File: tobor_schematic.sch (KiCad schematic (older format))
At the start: 19 parts

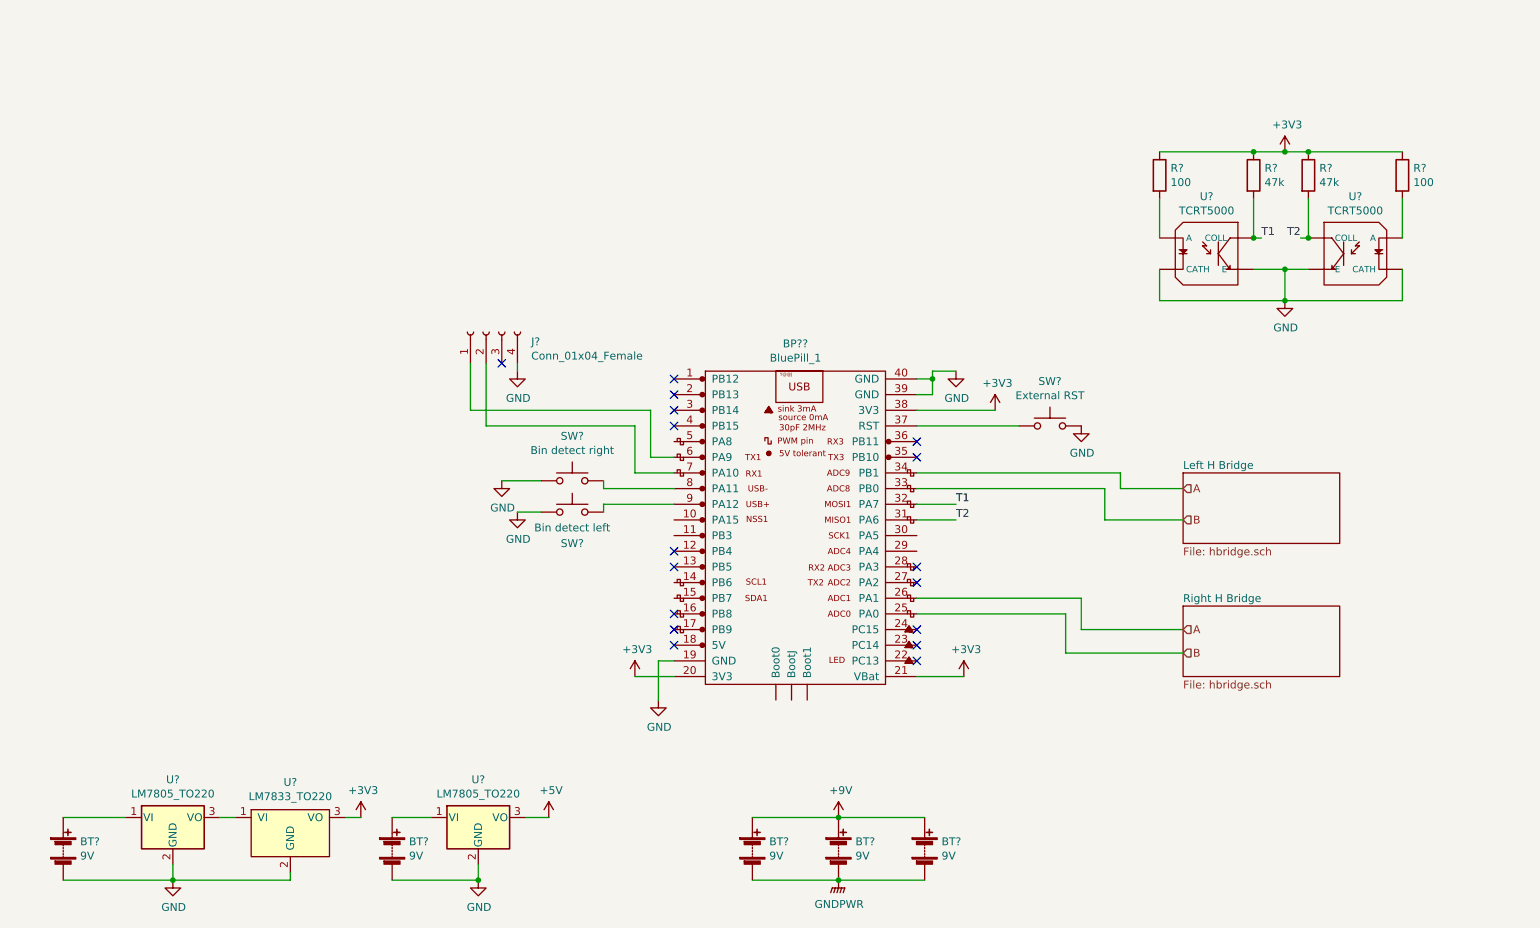
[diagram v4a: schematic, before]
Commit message: Add part numbers
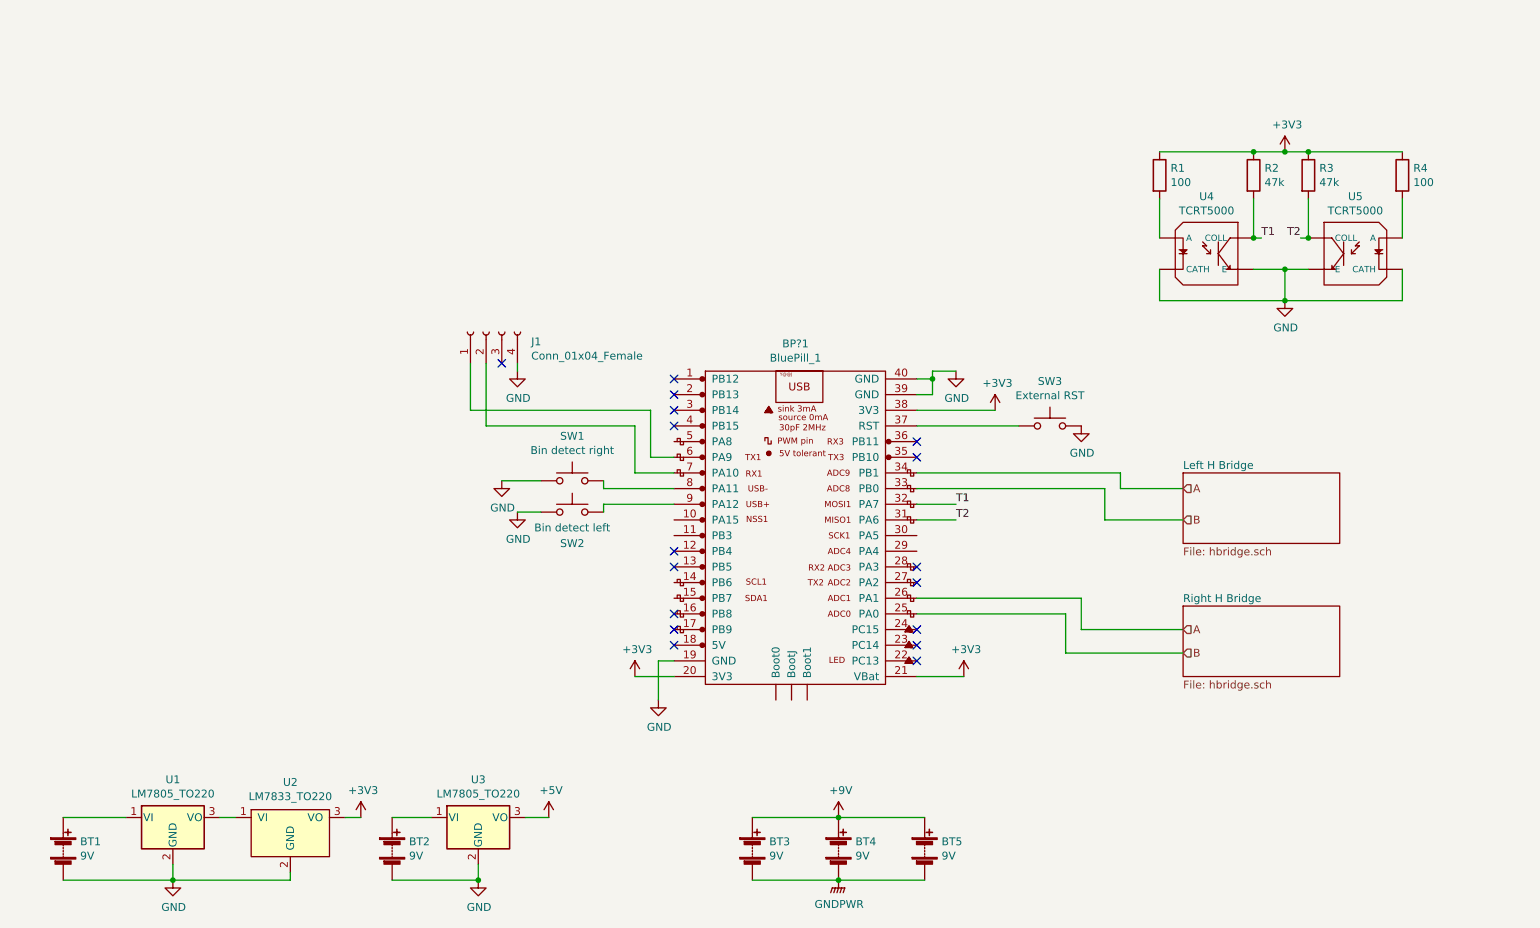
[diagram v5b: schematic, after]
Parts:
- gave numbers to parts that had none: 19
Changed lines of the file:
@@
 $EndDescr
 $Comp
-L Device:Battery BT?
+L Device:Battery BT1
 U 1 1 5EF5BD77
 P 1300 6050
-F 0 "BT?" H 1408 6096 50  0000 L CNN
+F 0 "BT1" H 1408 6096 50  0000 L CNN
 F 1 "9V" H 1408 6005 50  0000 L CNN
 F 2 "" V 1300 6110 50  0001 C CNN
@@
 $EndComp
 $Comp
-L Device:Battery BT?
+L Device:Battery BT3
 U 1 1 5EF5C6C1
 P 5700 6050
-F 0 "BT?" H 5808 6096 50  0000 L CNN
+F 0 "BT3" H 5808 6096 50  0000 L CNN
 F 1 "9V" H 5808 6005 50  0000 L CNN
 F 2 "" V 5700 6110 50  0001 C CNN
@@
 $EndComp
 $Comp
-L Device:Battery BT?
+L Device:Battery BT4
 U 1 1 5EF5C9BC
 P 6250 6050
-F 0 "BT?" H 6358 6096 50  0000 L CNN
+F 0 "BT4" H 6358 6096 50  0000 L CNN
 F 1 "9V" H 6358 6005 50  0000 L CNN
 F 2 "" V 6250 6110 50  0001 C CNN
@@
 $EndComp
 $Comp
-L Device:Battery BT?
+L Device:Battery BT5
 U 1 1 5EF5CE4D
 P 6800 6050
-F 0 "BT?" H 6908 6096 50  0000 L CNN
+F 0 "BT5" H 6908 6096 50  0000 L CNN
 F 1 "9V" H 6908 6005 50  0000 L CNN
 F 2 "" V 6800 6110 50  0001 C CNN
@@
 $EndComp
 $Comp
-L Device:Battery BT?
+L Device:Battery BT2
 U 1 1 5EF5D22E
 P 3400 6050
-F 0 "BT?" H 3508 6096 50  0000 L CNN
+F 0 "BT2" H 3508 6096 50  0000 L CNN
 F 1 "9V" H 3508 6005 50  0000 L CNN
 F 2 "" V 3400 6110 50  0001 C CNN
@@
 Connection ~ 6250 6250
 $Comp
-L Regulator_Linear:LM7805_TO220 U?
+L Regulator_Linear:LM7805_TO220 U1
 U 1 1 5EF5FC3A
 P 2000 5850
-F 0 "U?" H 2000 6092 50  0000 C CNN
+F 0 "U1" H 2000 6092 50  0000 C CNN
 F 1 "LM7805_TO220" H 2000 6001 50  0000 C CNN
 F 2 "Package_TO_SOT_THT:TO-220-3_Vertical" H 2000 6075 50  0001 C CIN
@@
 	2000 6250 2000 6150
 $Comp
-L Regulator_Linear:LM7805_TO220 U?
+L Regulator_Linear:LM7805_TO220 U3
 U 1 1 5EF6637D
 P 3950 5850
-F 0 "U?" H 3950 6092 50  0000 C CNN
+F 0 "U3" H 3950 6092 50  0000 C CNN
 F 1 "LM7805_TO220" H 3950 6001 50  0000 C CNN
 F 2 "Package_TO_SOT_THT:TO-220-3_Vertical" H 3950 6075 50  0001 C CIN
@@
 Connection ~ 3950 6250
 $Comp
-L tobor:LM7833_TO220 U?
+L tobor:LM7833_TO220 U2
 U 1 1 5EF8F890
 P 2750 5700
-F 0 "U?" H 2750 5775 50  0000 C CNN
+F 0 "U2" H 2750 5775 50  0000 C CNN
 F 1 "LM7833_TO220" H 2750 5684 50  0000 C CNN
 F 2 "" H 2750 5700 50  0001 C CNN
@@
 	6750 3950 7000 3950
 $Comp
-L Switch:SW_Push SW?
+L Switch:SW_Push SW1
 U 1 1 5EF80FC0
 P 4550 3700
-F 0 "SW?" H 4550 3985 50  0000 C CNN
+F 0 "SW1" H 4550 3985 50  0000 C CNN
 F 1 "Bin detect right" H 4550 3894 50  0000 C CNN
 F 2 "" H 4550 3900 50  0001 C CNN
@@
 $EndComp
 $Comp
-L Switch:SW_Push SW?
+L Switch:SW_Push SW2
 U 1 1 5EF82431
 P 4550 3900
-F 0 "SW?" H 4550 3700 50  0000 C CNN
+F 0 "SW2" H 4550 3700 50  0000 C CNN
 F 1 "Bin detect left" H 4550 3800 50  0000 C CNN
 F 2 "" H 4550 4100 50  0001 C CNN
@@
 NoConn ~ 5200 3350
 $Comp
-L STM32:BluePill_1 BP??
+L STM32:BluePill_1 BP?1
 U 1 1 5EF58E87
 P 5400 3000
-F 0 "BP??" H 5975 3175 50  0000 C CNN
+F 0 "BP?1" H 5975 3175 50  0000 C CNN
 F 1 "BluePill_1" H 5975 3084 50  0000 C CNN
 F 2 "" H 6650 1050 50  0001 C CNN
@@
 $EndComp
 $Comp
-L Switch:SW_Push SW?
+L Switch:SW_Push SW3
 U 1 1 5EF9F9FF
 P 7600 3350
-F 0 "SW?" H 7600 3635 50  0000 C CNN
+F 0 "SW3" H 7600 3635 50  0000 C CNN
 F 1 "External RST" H 7600 3544 50  0000 C CNN
 F 2 "" H 7600 3550 50  0001 C CNN
@@
 $EndComp
 $Comp
-L Connector:Conn_01x04_Female J?
+L Connector:Conn_01x04_Female J1
 U 1 1 5EFA8BEC
 P 4000 2750
-F 0 "J?" V 3938 2462 50  0000 R CNN
+F 0 "J1" V 3938 2462 50  0000 R CNN
 F 1 "Conn_01x04_Female" V 3847 2462 50  0000 R CNN
 F 2 "" H 4000 2750 50  0001 C CNN
@@
 	9250 1900 9250 2150
 $Comp
-L Device:R R?
+L Device:R R3
 U 1 1 5EF65A73
 P 9250 1750
-F 0 "R?" H 9320 1796 50  0000 L CNN
+F 0 "R3" H 9320 1796 50  0000 L CNN
 F 1 "47k" H 9320 1705 50  0000 L CNN
 F 2 "" V 9180 1750 50  0001 C CNN
@@
 $EndComp
 $Comp
-L Device:R R?
+L Device:R R4
 U 1 1 5EF65515
 P 9850 1750
-F 0 "R?" H 9920 1796 50  0000 L CNN
+F 0 "R4" H 9920 1796 50  0000 L CNN
 F 1 "100" H 9920 1705 50  0000 L CNN
 F 2 "" V 9780 1750 50  0001 C CNN
@@
 $EndComp
 $Comp
-L TCRT5000:TCRT5000 U?
+L TCRT5000:TCRT5000 U5
 U 1 1 5EF643B0
 P 9550 2250
-F 0 "U?" H 9550 2615 50  0000 C CNN
+F 0 "U5" H 9550 2615 50  0000 C CNN
 F 1 "TCRT5000" H 9550 2524 50  0000 C CNN
 F 2 "OPTO_TCRT5000" H 9550 2250 50  0001 L BNN
@@
 	8300 1900 8300 2150
 $Comp
-L Device:R R?
+L Device:R R2
 U 1 1 5EF5F885
 P 8900 1750
-F 0 "R?" H 8970 1796 50  0000 L CNN
+F 0 "R2" H 8970 1796 50  0000 L CNN
 F 1 "47k" H 8970 1705 50  0000 L CNN
 F 2 "" V 8830 1750 50  0001 C CNN
@@
 $EndComp
 $Comp
-L Device:R R?
+L Device:R R1
 U 1 1 5EF5F265
 P 8300 1750
-F 0 "R?" H 8370 1796 50  0000 L CNN
+F 0 "R1" H 8370 1796 50  0000 L CNN
 F 1 "100" H 8370 1705 50  0000 L CNN
 F 2 "" V 8230 1750 50  0001 C CNN
@@
 $EndComp
 $Comp
-L TCRT5000:TCRT5000 U?
+L TCRT5000:TCRT5000 U4
 U 1 1 5EF5CF42
 P 8600 2250
-F 0 "U?" H 8600 2615 50  0000 C CNN
+F 0 "U4" H 8600 2615 50  0000 C CNN
 F 1 "TCRT5000" H 8600 2524 50  0000 C CNN
 F 2 "OPTO_TCRT5000" H 8600 2250 50  0001 L BNN

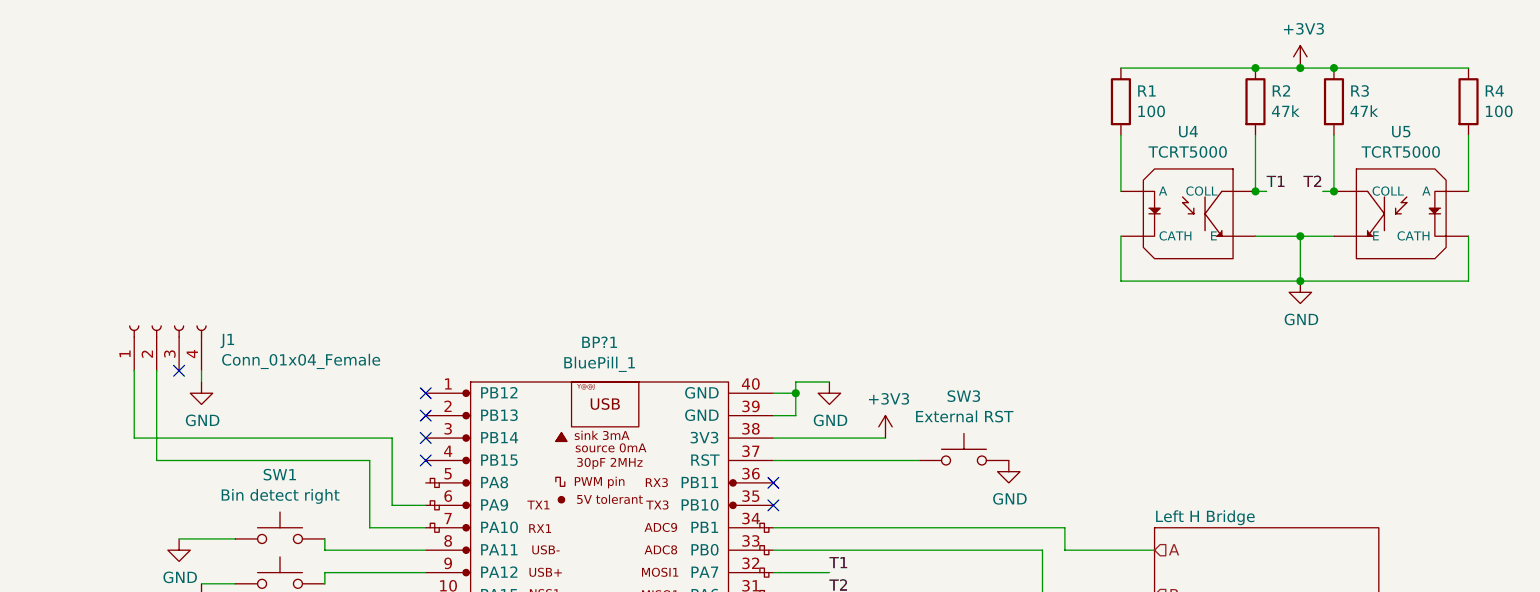
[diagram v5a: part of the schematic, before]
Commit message: Update tape sensor resistor values, fix programming connector
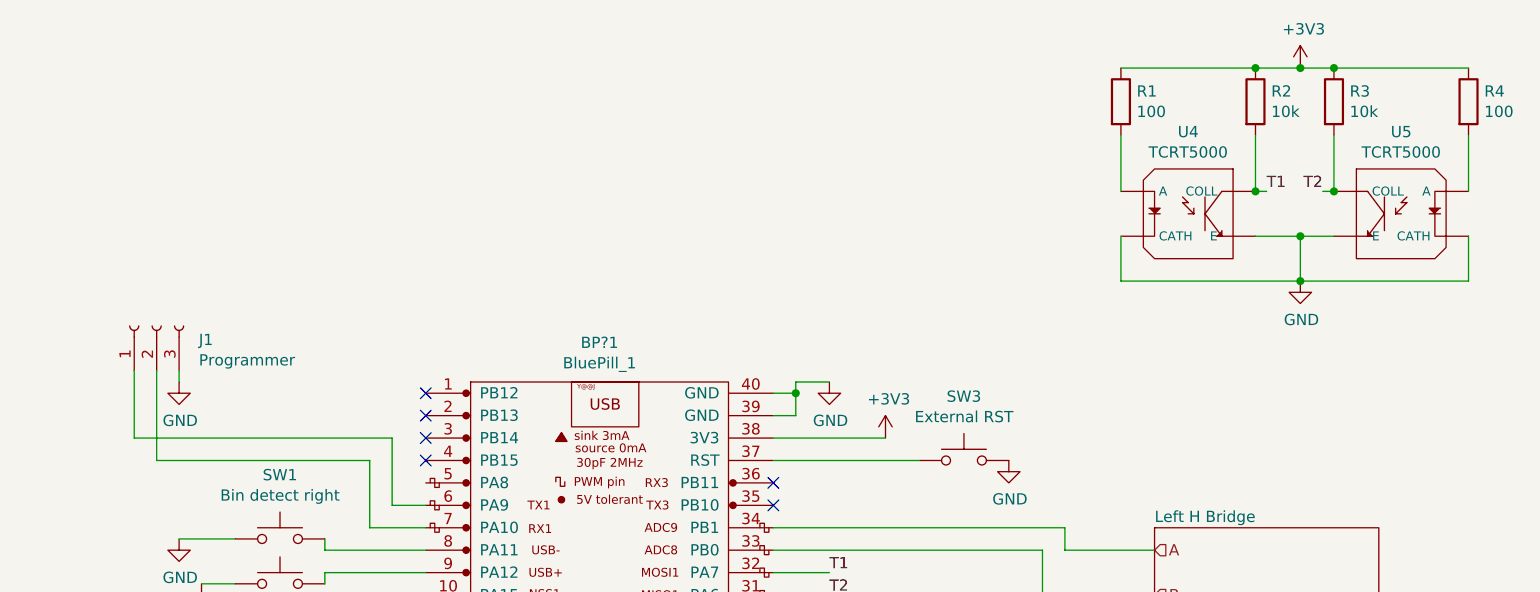
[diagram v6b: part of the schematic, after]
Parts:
- removed J1: Conn_01x04_Female, symbol Connector:Conn_01x04_Female
- added J1: Programmer, symbol Connector:Conn_01x03_Female
- R2, R3: value 47k -> 10k
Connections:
- net GND: now also J1.3 (Pin_3)
- net at BP?1.6 (PA9): now also J1.1 (Pin_1)
- net at BP?1.7 (PA10): now also J1.2 (Pin_2)
- no-connect marks 17 -> 16
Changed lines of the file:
@@
 	1    0    0    -1
-$EndComp
-$Comp
-L Connector:Conn_01x04_Female J1
-U 1 1 5EFA8BEC
-P 4000 2750
-F 0 "J1" V 3938 2462 50  0000 R CNN
-F 1 "Conn_01x04_Female" V 3847 2462 50  0000 R CNN
-F 2 "" H 4000 2750 50  0001 C CNN
-F 3 "~" H 4000 2750 50  0001 C CNN
-	1    4000 2750
-	0    -1   -1   0
 $EndComp
 Wire Wire Line
@@
 Wire Wire Line
 	3900 3250 3900 2950
-NoConn ~ 4100 2950
 $Comp
 L power:GND #PWR?
 U 1 1 5EFB4085
-P 4200 3000
-F 0 "#PWR?" H 4200 2750 50  0001 C CNN
-F 1 "GND" H 4205 2827 50  0000 C CNN
-F 2 "" H 4200 3000 50  0001 C CNN
-F 3 "" H 4200 3000 50  0001 C CNN
-	1    4200 3000
-	1    0    0    -1
-$EndComp
-Wire Wire Line
-	4200 3000 4200 2950
+P 4100 3000
+F 0 "#PWR?" H 4100 2750 50  0001 C CNN
+F 1 "GND" H 4105 2827 50  0000 C CNN
+F 2 "" H 4100 3000 50  0001 C CNN
+F 3 "" H 4100 3000 50  0001 C CNN
+	1    4100 3000
+	1    0    0    -1
+$EndComp
+Wire Wire Line
+	4100 3000 4100 2950
 $Comp
 L power:+9V #PWR?
@@
 P 9250 1750
 F 0 "R3" H 9320 1796 50  0000 L CNN
-F 1 "47k" H 9320 1705 50  0000 L CNN
+F 1 "10k" H 9320 1705 50  0000 L CNN
 F 2 "" V 9180 1750 50  0001 C CNN
 F 3 "~" H 9250 1750 50  0001 C CNN
@@
 P 8900 1750
 F 0 "R2" H 8970 1796 50  0000 L CNN
-F 1 "47k" H 8970 1705 50  0000 L CNN
+F 1 "10k" H 8970 1705 50  0000 L CNN
 F 2 "" V 8830 1750 50  0001 C CNN
 F 3 "~" H 8900 1750 50  0001 C CNN
@@
 Wire Wire Line
 	7700 4800 8450 4800
+$Comp
+L Connector:Conn_01x03_Female J1
+U 1 1 5EFC76D0
+P 4000 2750
+F 0 "J1" V 3938 2562 50  0000 R CNN
+F 1 "Programmer" V 3847 2562 50  0000 R CNN
+F 2 "" H 4000 2750 50  0001 C CNN
+F 3 "~" H 4000 2750 50  0001 C CNN
+	1    4000 2750
+	0    -1   -1   0
+$EndComp
 $EndSCHEMATC

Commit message: Add Nemo, relable Dory
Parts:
- added R13: 100, symbol Device:R
- added R14: 10k, symbol Device:R
- added U10: TCRT5000, OPTO_TCRT5000, symbol TCRT5000:TCRT5000
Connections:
- net +3V3: now also R13.1, R14.1
- net GND: now also U10.CATH, U10.E
- net N: now reaches BP?1.28 (PA3)
- net N: now also R14.2, U10.C (COLL)
- new net: R13.2, U10.A
- no-connect marks 16 -> 15
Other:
- note added: "Dory"
- note added: "Nemo"
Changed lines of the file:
@@
 NoConn ~ 6750 4650
 NoConn ~ 6750 4350
-NoConn ~ 6750 4250
 NoConn ~ 6750 3550
 NoConn ~ 6750 3450
@@
 Wire Wire Line
 	9250 2150 9200 2150
-Text Label 8950 2150 0    50   ~ 0
-T1
 Connection ~ 8900 2150
 Wire Wire Line
@@
 	0    -1   -1   0
 $EndComp
+Text Notes 8200 1300 0    50   ~ 0
+Dory
+Wire Notes Line
+	8150 1350 10150 1350
+Wire Notes Line
+	10150 1350 10150 2850
+Wire Notes Line
+	10150 2850 8150 2850
+Wire Notes Line
+	8150 2850 8150 1350
+$Comp
+L TCRT5000:TCRT5000 U10
+U 1 1 5F00A78B
+P 6800 2300
+F 0 "U10" H 6800 2665 50  0000 C CNN
+F 1 "TCRT5000" H 6800 2574 50  0000 C CNN
+F 2 "OPTO_TCRT5000" H 6800 2300 50  0001 L BNN
+F 3 "Vishay" H 6800 2300 50  0001 L BNN
+F 4 "7.2mm" H 6800 2300 50  0001 L BNN "Field4"
+F 5 "Manufacturer recommendations" H 6800 2300 50  0001 L BNN "Field5"
+F 6 "1.7" H 6800 2300 50  0001 L BNN "Field6"
+	1    6800 2300
+	1    0    0    -1
+$EndComp
+$Comp
+L power:GND #PWR?
+U 1 1 5F011CDC
+P 6800 2650
+F 0 "#PWR?" H 6800 2400 50  0001 C CNN
+F 1 "GND" H 6805 2477 50  0000 C CNN
+F 2 "" H 6800 2650 50  0001 C CNN
+F 3 "" H 6800 2650 50  0001 C CNN
+	1    6800 2650
+	1    0    0    -1
+$EndComp
+Wire Wire Line
+	6500 2400 6500 2650
+Wire Wire Line
+	6500 2650 6800 2650
+Wire Wire Line
+	6800 2650 7100 2650
+Wire Wire Line
+	7100 2650 7100 2400
+Connection ~ 6800 2650
+$Comp
+L Device:R R13
+U 1 1 5F015A8B
+P 6500 1750
+F 0 "R13" H 6570 1796 50  0000 L CNN
+F 1 "100" H 6570 1705 50  0000 L CNN
+F 2 "" V 6430 1750 50  0001 C CNN
+F 3 "~" H 6500 1750 50  0001 C CNN
+	1    6500 1750
+	1    0    0    -1
+$EndComp
+Wire Wire Line
+	6500 1900 6500 2200
+$Comp
+L Device:R R14
+U 1 1 5F018676
+P 7100 1750
+F 0 "R14" H 7170 1796 50  0000 L CNN
+F 1 "10k" H 7170 1705 50  0000 L CNN
+F 2 "" V 7030 1750 50  0001 C CNN
+F 3 "~" H 7100 1750 50  0001 C CNN
+	1    7100 1750
+	1    0    0    -1
+$EndComp
+$Comp
+L power:+3V3 #PWR?
+U 1 1 5F01B430
+P 6800 1600
+F 0 "#PWR?" H 6800 1450 50  0001 C CNN
+F 1 "+3V3" H 6815 1773 50  0000 C CNN
+F 2 "" H 6800 1600 50  0001 C CNN
+F 3 "" H 6800 1600 50  0001 C CNN
+	1    6800 1600
+	1    0    0    -1
+$EndComp
+Wire Wire Line
+	6500 1600 6800 1600
+Connection ~ 6800 1600
+Wire Wire Line
+	6800 1600 7100 1600
+Wire Notes Line
+	7350 1350 7350 2900
+Wire Notes Line
+	6350 2900 6350 1350
+Text Notes 6450 1300 0    50   ~ 0
+Nemo
+Wire Notes Line
+	6350 1350 7350 1350
+Wire Notes Line
+	7350 2900 6350 2900
+Text Label 7150 2200 0    50   ~ 0
+N
+Text Label 7000 4250 0    50   ~ 0
+N
+Text Label 8950 2150 0    50   ~ 0
+T1
+Wire Wire Line
+	7000 4250 6750 4250
+Wire Wire Line
+	7100 1900 7100 2200
+Wire Wire Line
+	7100 2200 7150 2200
+Connection ~ 7100 2200
 $EndSCHEMATC
